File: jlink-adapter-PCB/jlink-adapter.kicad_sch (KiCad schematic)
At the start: 13 parts, among them J1 Conn_02x10_Odd_Even, J2 Conn_02x05_Odd_Even, J3 Tag-Connect IDC, Q1 BSS123TA

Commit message: Update Jlink to clear ERC issues
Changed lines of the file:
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@@
+	)
+	(junction
+		(at 203.2 31.75)
+		(diameter 0)
+		(color 0 0 0 0)
 	)
 	(junction
@@
 	(wire
 		(pts
+			(xy 203.2 31.75) (xy 207.01 31.75)
+		)
+		(stroke
+			(width 0)
+			(type default)
+		)
+	)
+	(wire
+		(pts
 			(xy 219.71 39.37) (xy 228.6 39.37)
 		)
@@
 	(wire
 		(pts
+			(xy 133.35 27.94) (xy 140.97 27.94)
+		)
+		(stroke
+			(width 0)
+			(type default)
+		)
+	)
+	(wire
+		(pts
 			(xy 151.13 44.45) (xy 160.02 44.45)
 		)
@@
 	(wire
 		(pts
-			(xy 199.39 31.75) (xy 207.01 31.75)
-		)
-		(stroke
-			(width 0)
-			(type default)
-		)
-	)
-	(wire
-		(pts
 			(xy 140.97 27.94) (xy 140.97 29.21)
+		)
+		(stroke
+			(width 0)
+			(type default)
+		)
+	)
+	(wire
+		(pts
+			(xy 194.31 31.75) (xy 203.2 31.75)
 		)
 		(stroke
@@
 	)
 	(label "VTREF"
-		(at 140.97 27.94 0)
+		(at 133.35 27.94 0)
 		(fields_autoplaced yes)
 		(effects
@@
 	)
 	(label "VTREF"
-		(at 199.39 31.75 0)
+		(at 194.31 31.75 0)
 		(fields_autoplaced yes)
 		(effects
@@
 			)
 		)
-		(property "Description" ""
+		(property "Description" "Power symbol creates a global label with name \"GND\" , ground"
 			(at 130.81 140.97 0)
 			(effects
@@
 			)
 		)
-		(property "Description" ""
+		(property "Description" "Power symbol creates a global label with name \"GND\" , ground"
 			(at 140.97 50.8 0)
 			(effects
@@
 			)
 		)
-		(property "Description" ""
+		(property "Description" "Power symbol creates a global label with name \"+5V\""
 			(at 130.81 95.25 0)
 			(effects
@@
 			)
 		)
-		(property "Description" ""
+		(property "Description" "Power symbol creates a global label with name \"+5V\""
 			(at 34.29 43.18 0)
 			(effects
@@
 			)
 		)
-		(property "Description" ""
+		(property "Description" "Power symbol creates a global label with name \"GND\" , ground"
 			(at 193.04 44.45 0)
 			(effects
@@
 			)
 		)
-		(property "Description" ""
+		(property "Description" "Power symbol creates a global label with name \"GND\" , ground"
 			(at 107.95 146.05 0)
 			(effects
@@
 			)
 		)
-		(property "Description" ""
+		(property "Description" "Power symbol creates a global label with name \"GND\" , ground"
 			(at 40.64 140.97 0)
 			(effects
@@
 			)
 		)
-		(property "Description" ""
+		(property "Description" "Power symbol creates a global label with name \"GND\" , ground"
 			(at 120.65 146.05 0)
 			(effects
@@
 			)
 		)
-		(property "Description" ""
+		(property "Description" "Power symbol creates a global label with name \"GND\" , ground"
 			(at 71.12 44.45 0)
 			(effects
@@
 			)
 		)
-		(property "Description" ""
+		(property "Description" "Power symbol creates a global label with name \"+5V\""
 			(at 40.64 105.41 0)
 			(effects
@@
 					(unit 1)
 				)
+			)
+		)
+	)
+	(symbol
+		(lib_id "power:PWR_FLAG")
+		(at 203.2 31.75 0)
+		(unit 1)
+		(exclude_from_sim no)
+		(in_bom yes)
+		(on_board yes)
+		(dnp no)
+		(fields_autoplaced yes)
+		(property "Reference" "#FLG03"
+			(at 203.2 29.845 0)
+			(effects
+				(font
+					(size 1.27 1.27)
+				)
+				(hide yes)
+			)
+		)
+		(property "Value" "PWR_FLAG"
+			(at 203.2 26.67 0)
+			(effects
+				(font
+					(size 1.27 1.27)
+				)
+				(hide yes)
+			)
+		)
+		(property "Footprint" ""
+			(at 203.2 31.75 0)
+			(effects
+				(font
+					(size 1.27 1.27)
+				)
+				(hide yes)
+			)
+		)
+		(property "Datasheet" "~"
+			(at 203.2 31.75 0)
+			(effects
+				(font
+					(size 1.27 1.27)
+				)
+				(hide yes)
+			)
+		)
+		(property "Description" "Special symbol for telling ERC where power comes from"
+			(at 203.2 31.75 0)
+			(effects
+				(font
+					(size 1.27 1.27)
+				)
+				(hide yes)
+			)
+		)
+		(pin "1"
+		)
+		(instances
+			(project "jlink-adapter"
+				(path "/c4b4938f-57db-4256-8168-815a3371e956"
+					(reference "#FLG03")
+					(unit 1)
+				)

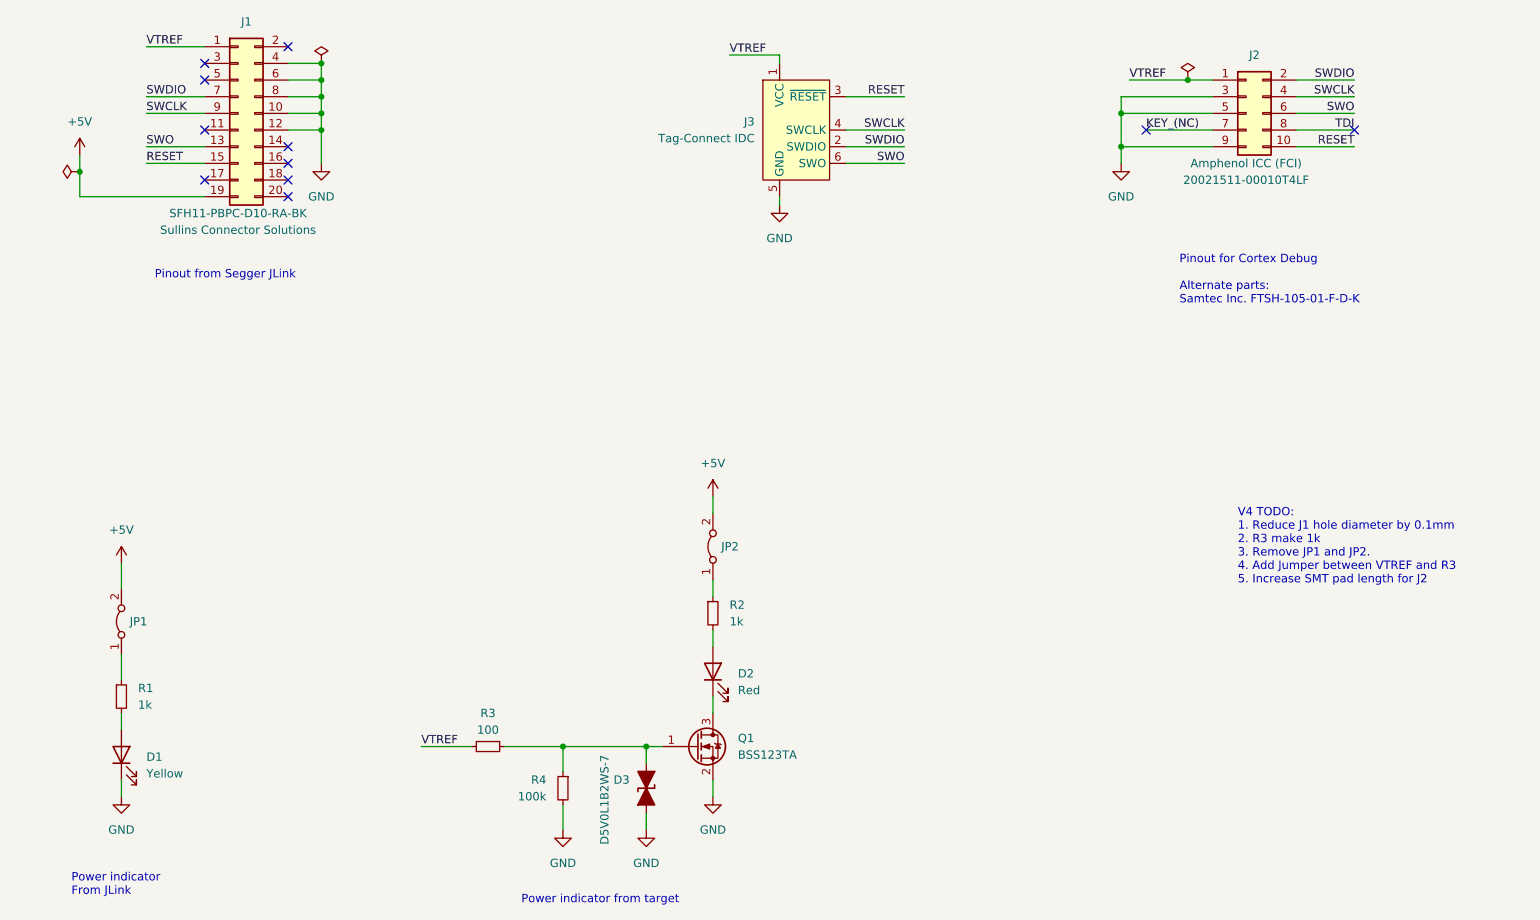
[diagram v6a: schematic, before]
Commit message: Add features and minor improvements from V4
* Add Custom Segger Adapter
* Add a 5V tap off point
* Add a reset button for the MCU
* Remove Jumpers
* Swapped the Inner Plane to supply Vtref, rather than 5V, as 5V goes to fewer places.
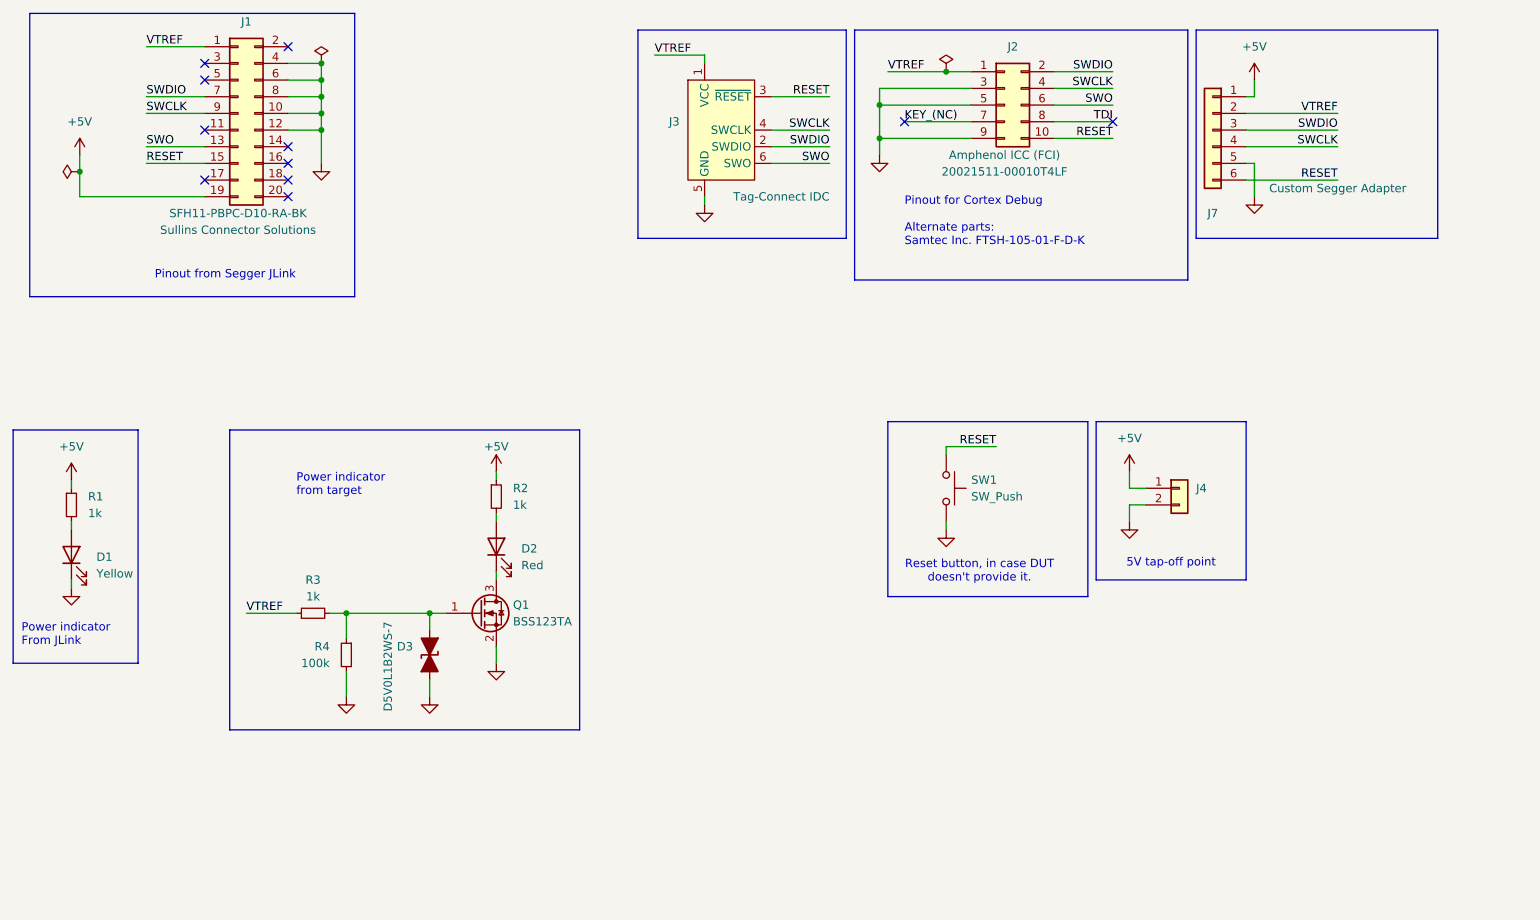
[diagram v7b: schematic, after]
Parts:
- removed JP1, JP2: Jumper_2_Bridged, Jumper:SolderJumper-2_P1.3mm_Bridged_RoundedPad1.0x1.5mm, symbol Jumper:Jumper_2_Bridged
- added J4: Conn_01x02, Connector_PinSocket_2.54mm:PinSocket_1x02_P2.54mm_Vertical, symbol Connector_Generic:Conn_01x02
- added J7: Custom Segger Adapter, Connector_PinHeader_1.27mm:PinHeader_1x06_P1.27mm_Vertical, symbol Connector_Generic:Conn_01x06
- added SW1: SW_Push, Button_Switch_SMD:SW_SPST_TL3305B, symbol Switch:SW_Push
- Q1: symbol Device:Q_NMOS_GSD -> Transistor_FET:Q_NMOS_GSD
- R3: value 100 -> 1k
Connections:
- net +5V: now also R1.1, R2.1, J4.1 (Pin_1), J7.1 (Pin_1)
- net GND: now also J4.2 (Pin_2), J7.5 (Pin_5), SW1.2
- net RESET: now also J7.6 (Pin_6), SW1.1
- net SWCLK: now also J7.4 (Pin_4)
- net SWDIO: now also J7.3 (Pin_3)
- net VTREF: now also J7.2 (Pin_2)
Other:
- note added: "5V tap-off point"
- note added: "Reset button, in case DUT doesn't provide it."
- note removed: "V4 TODO: 1. Reduce J1 hole diameter by 0.1mm 2. R3 make 1k 3. Remove JP1 and JP2. 4. Add Jumper between VTREF and R3 5. Increase SMT pad length for J2"
- moved on the sheet: D1, D2, D3, J2, J3, Q1, R1, R2, R3, R4
